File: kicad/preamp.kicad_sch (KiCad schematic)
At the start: 18 parts, among them Q1 MMBF5457, Q2 MMBF5457

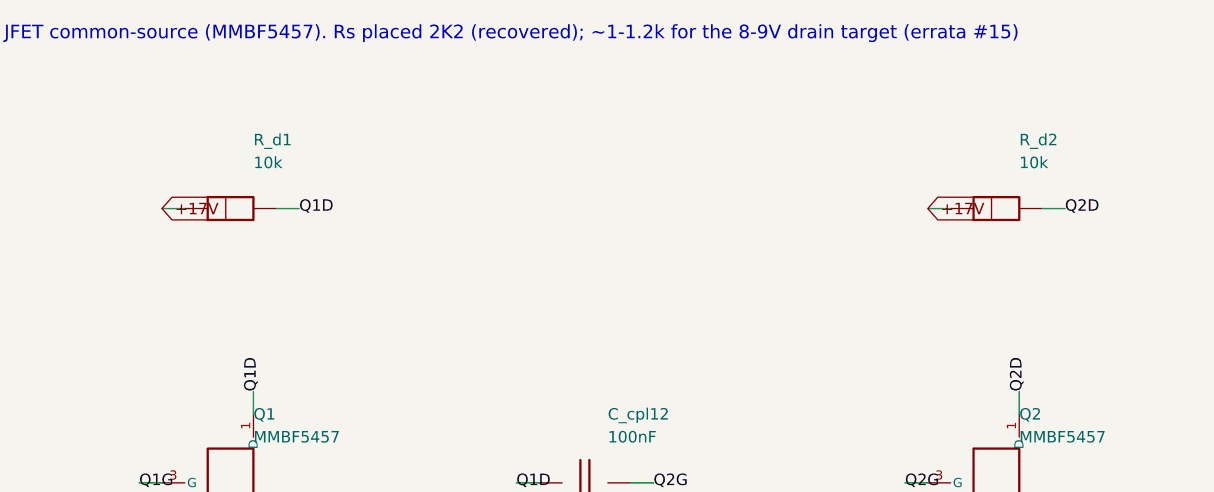
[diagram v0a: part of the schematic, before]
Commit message: Noise, hum, crosstalk and thermal models; three design fixes; JLCPCB rules and cost
New models (docs/06c, spice/): a .noise run of the whole front end including the
LM317's own rail noise, the rail-ripple paths to the speaker, a vactrol-level tremolo
depth model, an electro-thermal LM1875 ladder, and a geometric crosstalk audit of the
routed boards (kicad/gen/crosstalk_audit.py). They found three defects:

- Errata #21 (hum + hiss): the LM1875 bias divider had no bypass (+4 dB ripple to
  speaker, 0.4 Vrms of 100 Hz at idle) and the LM317's 0.5 mV of noise reached the
  0 dB-PSRR JFET stages (23 dB above their floor, SNR 34 dB). Fixed with C_bref +
  R_bias3 on the power amp, C_adj on the regulator, and an RC-decoupled +17V_PRE rail
  for Q1/Q2/Q_rec: hum 408 mV -> 0.3 mV, EIN 37 -> 2.7 uV, SNR 34 -> 57 dB.
- Errata #22 (tremolo depth 1.7 dB): the vactrol LED was returned to ground from a
  mid-rail LFO -> 7 mA DC, a fixed -20 dB pad. LED limiter (2 V swing, LED_rate is one
  limiter LED) + Q_trem 2N3904/MMBT3904 emitter follower AC-coupled from the depth
  pot -> 15 dB depth, 0.8 dB insertion loss.
- Errata #23 (fab): stock TO-92 and the LM1875 footprint were under JLCPCB's 0.18 mm
  annular-ring minimum -> TO-92_Inline_Wide and 1.5 mm LM1875 pads; both .kicad_pro
  carry JLC's 2-layer limits as DRC constraints. Cost: all SMD caps 1206 (basic
  library), "(opt)" MRB caps DNP, gyrator on E24 values (same 1.86 H): 7 -> 2
  extended part types, ~$32 -> ~$17 assembly for five boards (kicad/gen/jlc_cost.py);
  three fiducials on the SMD board.

Crosstalk -> two routing rules (.kicad_dru: HighCurrent 0.6/0.4 mm and TankDrive
1.2/0.8 mm from signal copper, THT/SMD) that route_board.py also hands the router as
class clearances; keepout rule areas along the edge and around the mounting holes.
Thermal: Part 5's <= 2.5 K/W heatsink confirmed with numbers (Tj 97 C at 40 C ambient,
worst-case sine; 8-10 K/W clip-ons reach shutdown).

Placer: short parts stack beside tall ones i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
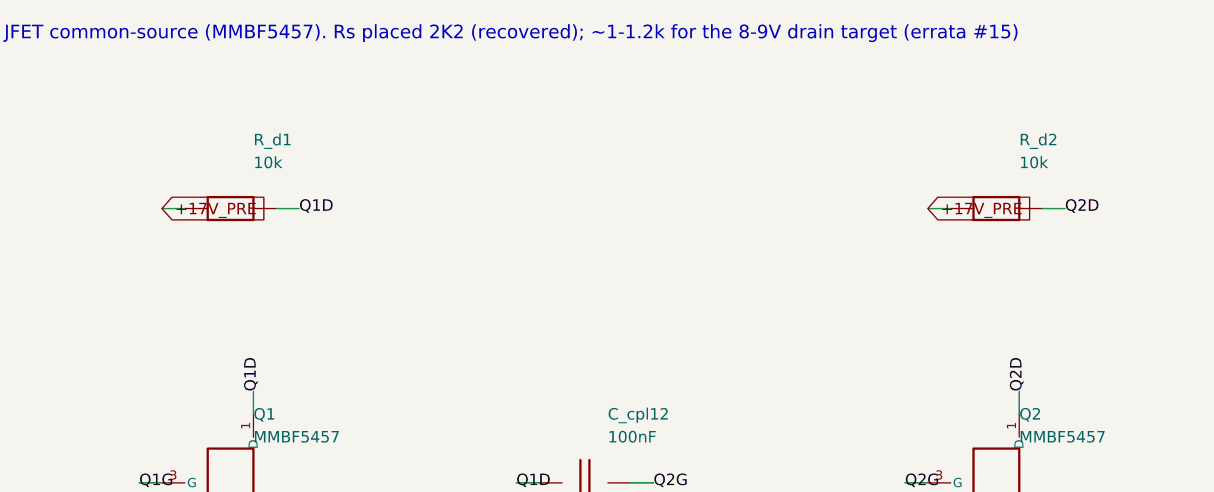
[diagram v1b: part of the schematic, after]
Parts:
- Q1, Q2: footprint Package_TO_SOT_THT:TO-92_Inline -> Package_TO_SOT_THT:TO-92_Inline_Wide
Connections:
- net +17V renamed +17V_PRE
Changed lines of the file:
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@@
     (pin "1")
     (pin "2")
-    (instances (project "cambridge_reverb" (path "/fc10e795-2655-43ed-88d6-50e214c3afc4" (reference "C_in_pre") (unit 1))))
+    (instances (project "cambridge_reverb" (path "/a0cf396d-e505-46cc-81e6-43b449fe841c" (reference "C_in_pre") (unit 1))))
   )
   (wire (pts (xy 116.84 53.339999999999996) (xy 114.3 53.339999999999996)) (stroke (width 0) (type default)))
@@
     (pin "1")
     (pin "2")
-    (instances (project "cambridge_reverb" (path "/fc10e795-2655-43ed-88d6-50e214c3afc4" (reference "R_g1") (unit 1))))
+    (instances (project "cambridge_reverb" (path "/a0cf396d-e505-46cc-81e6-43b449fe841c" (reference "R_g1") (unit 1))))
   )
   (wire (pts (xy 116.84 83.82000000000001) (xy 114.3 83.82000000000001)) (stroke (width 0) (type default)))
@@
     (property "Reference" "Q1" (at 175.26 55.879999999999995 0) (effects (font (size 1.27 1.27)) (justify left)))
     (property "Value" "MMBF5457" (at 175.26 58.419999999999995 0) (effects (font (size 1.27 1.27)) (justify left)))
-    (property "Footprint" "Package_TO_SOT_THT:TO-92_Inline" (at 172.72 63.49999999999999 0) (effects (font (size 1.27 1.27)) hide))
+    (property "Footprint" "Package_TO_SOT_THT:TO-92_Inline_Wide" (at 172.72 63.49999999999999 0) (effects (font (size 1.27 1.27)) hide))
     (pin "3")
     (pin "1")
     (pin "2")
-    (instances (project "cambridge_reverb" (path "/fc10e795-2655-43ed-88d6-50e214c3afc4" (reference "Q1") (unit 1))))
+    (instances (project "cambridge_reverb" (path "/a0cf396d-e505-46cc-81e6-43b449fe841c" (reference "Q1") (unit 1))))
   )
   (wire (pts (xy 165.1 63.49999999999999) (xy 162.56 63.49999999999999)) (stroke (width 0) (type default)))
@@
     (pin "1")
     (pin "2")
-    (instances (project "cambridge_reverb" (path "/fc10e795-2655-43ed-88d6-50e214c3afc4" (reference "R_d1") (unit 1))))
+    (instances (project "cambridge_reverb" (path "/a0cf396d-e505-46cc-81e6-43b449fe841c" (reference "R_d1") (unit 1))))
   )
   (wire (pts (xy 167.64 33.019999999999996) (xy 165.1 33.019999999999996)) (stroke (width 0) (type default)))
-  (global_label "+17V" (shape input) (at 165.1 33.019999999999996 180) (fields_autoplaced) (effects (font (size 1.27 1.27)) (justify left)))
+  (global_label "+17V_PRE" (shape input) (at 165.1 33.019999999999996 180) (fields_autoplaced) (effects (font (size 1.27 1.27)) (justify left)))
   (wire (pts (xy 177.8 33.019999999999996) (xy 180.34 33.019999999999996)) (stroke (width 0) (type default)))
   (label "Q1D" (at 180.34 33.019999999999996 0) (effects (font (size 1.27 1.27)) (justify left)))
@@
     (pin "1")
     (pin "2")
-    (instances (project "cambridge_reverb" (path "/fc10e795-2655-43ed-88d6-50e214c3afc4" (reference "R_s1") (unit 1))))
+    (instances (project "cambridge_reverb" (path "/a0cf396d-e505-46cc-81e6-43b449fe841c" (reference "R_s1") (unit 1))))
   )
   (wire (pts (xy 167.64 104.14) (xy 165.1 104.14)) (stroke (width 0) (type default)))
@@
     (pin "1")
     (pin "2")
-    (instances (project "cambridge_reverb" (path "/fc10e795-2655-43ed-88d6-50e214c3afc4" (reference "C_s1") (unit 1))))
+    (instances (project "cambridge_reverb" (path "/a0cf396d-e505-46cc-81e6-43b449fe841c" (reference "C_s1") (unit 1))))
   )
   (wire (pts (xy 207.01 104.14) (xy 204.46999999999997 104.14)) (stroke (width 0) (type default)))
@@
     (pin "1")
     (pin "2")
-    (instances (project "cambridge_reverb" (path "/fc10e795-2655-43ed-88d6-50e214c3afc4" (reference "C_cpl12") (unit 1))))
+    (instances (project "cambridge_reverb" (path "/a0cf396d-e505-46cc-81e6-43b449fe841c" (reference "C_cpl12") (unit 1))))
   )
   (wire (pts (xy 207.01 63.49999999999999) (xy 204.46999999999997 63.49999999999999)) (stroke (width 0) (type default)))
@@
     (pin "1")
     (pin "2")
-    (instances (project "cambridge_reverb" (path "/fc10e795-2655-43ed-88d6-50e214c3afc4" (reference "R_g2") (unit 1))))
+    (instances (project "cambridge_reverb" (path "/a0cf396d-e505-46cc-81e6-43b449fe841c" (reference "R_g2") (unit 1))))
   )
   (wire (pts (xy 207.01 88.9) (xy 204.46999999999997 88.9)) (stroke (width 0) (type default)))
@@
     (property "Reference" "Q2" (at 260.35 55.879999999999995 0) (effects (font (size 1.27 1.27)) (justify left)))
     (property "Value" "MMBF5457" (at 260.35 58.419999999999995 0) (effects (font (size 1.27 1.27)) (justify left)))
-    (property "Footprint" "Package_TO_SOT_THT:TO-92_Inline" (at 257.81 63.49999999999999 0) (effects (font (size 1.27 1.27)) hide))
+    (property "Footprint" "Package_TO_SOT_THT:TO-92_Inline_Wide" (at 257.81 63.49999999999999 0) (effects (font (size 1.27 1.27)) hide))
     (pin "3")
     (pin "1")
     (pin "2")
-    (instances (project "cambridge_reverb" (path "/fc10e795-2655-43ed-88d6-50e214c3afc4" (reference "Q2") (unit 1))))
+    (instances (project "cambridge_reverb" (path "/a0cf396d-e505-46cc-81e6-43b449fe841c" (reference "Q2") (unit 1))))
   )
   (wire (pts (xy 250.19 63.49999999999999) (xy 247.64999999999998 63.49999999999999)) (stroke (width 0) (type default)))
@@
     (pin "1")
     (pin "2")
-    (instances (project "cambridge_reverb" (path "/fc10e795-2655-43ed-88d6-50e214c3afc4" (reference "R_d2") (unit 1))))
+    (instances (project "cambridge_reverb" (path "/a0cf396d-e505-46cc-81e6-43b449fe841c" (reference "R_d2") (unit 1))))
   )
   (wire (pts (xy 252.72999999999996 33.019999999999996) (xy 250.19 33.019999999999996)) (stroke (width 0) (type default)))
-  (global_label "+17V" (shape input) (at 250.19 33.019999999999996 180) (fields_autoplaced) (effects (font (size 1.27 1.27)) (justify left)))
+  (global_label "+17V_PRE" (shape input) (at 250.19 33.019999999999996 180) (fields_autoplaced) (effects (font (size 1.27 1.27)) (justify left)))
   (wire (pts (xy 262.89 33.019999999999996) (xy 265.43 33.019999999999996)) (stroke (width 0) (type default)))
   (label "Q2D" (at 265.43 33.019999999999996 0) (effects (font (size 1.27 1.27)) (justify left)))
@@
     (pin "1")
     (pin "2")
-    (instances (project "cambridge_reverb" (path "/fc10e795-2655-43ed-88d6-50e214c3afc4" (reference "C_pres") (unit 1))))
+    (instances (project "cambridge_reverb" (path "/a0cf396d-e505-46cc-81e6-43b449fe841c" (reference "C_pres") (unit 1))))
   )
   (wire (pts (xy 252.72999999999996 104.14) (xy 250.19 104.14)) (stroke (width 0) (type default)))
@@
     (pin "1")
     (pin "2")
-    (instances (project "cambridge_reverb" (path "/fc10e795-2655-43ed-88d6-50e214c3afc4" (reference "R_s2") (unit 1))))
+    (instances (project "cambridge_reverb" (path "/a0cf396d-e505-46cc-81e6-43b449fe841c" (reference "R_s2") (unit 1))))
   )
   (wire (pts (xy 292.09999999999997 88.9) (xy 289.56 88.9)) (stroke (width 0) (type default)))
@@
     (pin "1")
     (pin "2")
-    (instances (project "cambridge_reverb" (path "/fc10e795-2655-43ed-88d6-50e214c3afc4" (reference "C_s2") (unit 1))))
+    (instances (project "cambridge_reverb" (path "/a0cf396d-e505-46cc-81e6-43b449fe841c" (reference "C_s2") (unit 1))))
   )
   (wire (pts (xy 292.09999999999997 113.03) (xy 289.56 113.03)) (stroke (width 0) (type default)))
@@
     (pin "1")
     (pin "2")
-    (instances (project "cambridge_reverb" (path "/fc10e795-2655-43ed-88d6-50e214c3afc4" (reference "C_cpl_out") (unit 1))))
+    (instances (project "cambridge_reverb" (path "/a0cf396d-e505-46cc-81e6-43b449fe841c" (reference "C_cpl_out") (unit 1))))
   )
   (wire (pts (xy 292.09999999999997 48.26) (xy 289.56 48.26)) (stroke (width 0) (type default)))
@@
     (property "Footprint" "cambridge_reverb:TestPoint_THT_D2.0mm_Label" (at 121.91999999999999 243.84 0) (effects (font (size 1.27 1.27)) hide))
     (pin "1")
-    (instances (project "cambridge_reverb" (path "/fc10e795-2655-43ed-88d6-50e214c3afc4" (reference "TP_Q1D") (unit 1))))
+    (instances (project "cambridge_reverb" (path "/a0cf396d-e505-46cc-81e6-43b449fe841c" (reference "TP_Q1D") (unit 1))))
   )
   (wire (pts (xy 121.91999999999999 246.38) (xy 121.91999999999999 248.92)) (stroke (width 0) (type default)))
@@
     (property "Footprint" "cambridge_reverb:TestPoint_THT_D2.0mm_Label" (at 147.32 243.84 0) (effects (font (size 1.27 1.27)) hide))
     (pin "1")
-    (instances (project "cambridge_reverb" (path "/fc10e795-2655-43ed-88d6-50e214c3afc4" (reference "TP_Q2D") (unit 1))))
+    (instances (project "cambridge_reverb" (path "/a0cf396d-e505-46cc-81e6-43b449fe841c" (reference "TP_Q2D") (unit 1))))
   )
   (wire (pts (xy 147.32 246.38) (xy 147.32 248.92)) (stroke (width 0) (type default)))
@@
     (property "Footprint" "cambridge_reverb:TestPoint_THT_D2.0mm_Label" (at 172.72 243.84 0) (effects (font (size 1.27 1.27)) hide))
     (pin "1")
-    (instances (project "cambridge_reverb" (path "/fc10e795-2655-43ed-88d6-50e214c3afc4" (reference "TP_PRE_OUT") (unit 1))))
+    (instances (project "cambridge_reverb" (path "/a0cf396d-e505-46cc-81e6-43b449fe841c" (reference "TP_PRE_OUT") (unit 1))))
   )
   (wire (pts (xy 172.72 246.38) (xy 172.72 248.92)) (stroke (width 0) (type default)))
@@
     (property "Footprint" "cambridge_reverb:TestPoint_THT_D2.0mm_Label" (at 198.12 243.84 0) (effects (font (size 1.27 1.27)) hide))
     (pin "1")
-    (instances (project "cambridge_reverb" (path "/fc10e795-2655-43ed-88d6-50e214c3afc4" (reference "TP_GND_PRE") (unit 1))))
+    (instances (project "cambridge_reverb" (path "/a0cf396d-e505-46cc-81e6-43b449fe841c" (reference "TP_GND_PRE") (unit 1))))
   )
   (wire (pts (xy 198.12 246.38) (xy 198.12 248.92)) (stroke (width 0) (type default)))
